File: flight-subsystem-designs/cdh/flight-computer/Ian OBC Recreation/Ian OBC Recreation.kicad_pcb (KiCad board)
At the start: 4 copper layers, 90 x 96 mm, 43 parts, among them J1 Conn_01x03, J2 Conn_01x03, J3 Conn_01x03, J4 Conn_01x03, J5 Conn_01x03, J6 Conn_01x03, J8 Conn_02x26_Odd_Even, Q1 AON6411, U1 BEAGLEBONEBLACK, U2 TPS2400DBVR, U3 TCAN337G, U4 MCP7940N-xSN, U5 ADM3485EARZ, U6 MAX706RESA+T, U7 TMP36xS

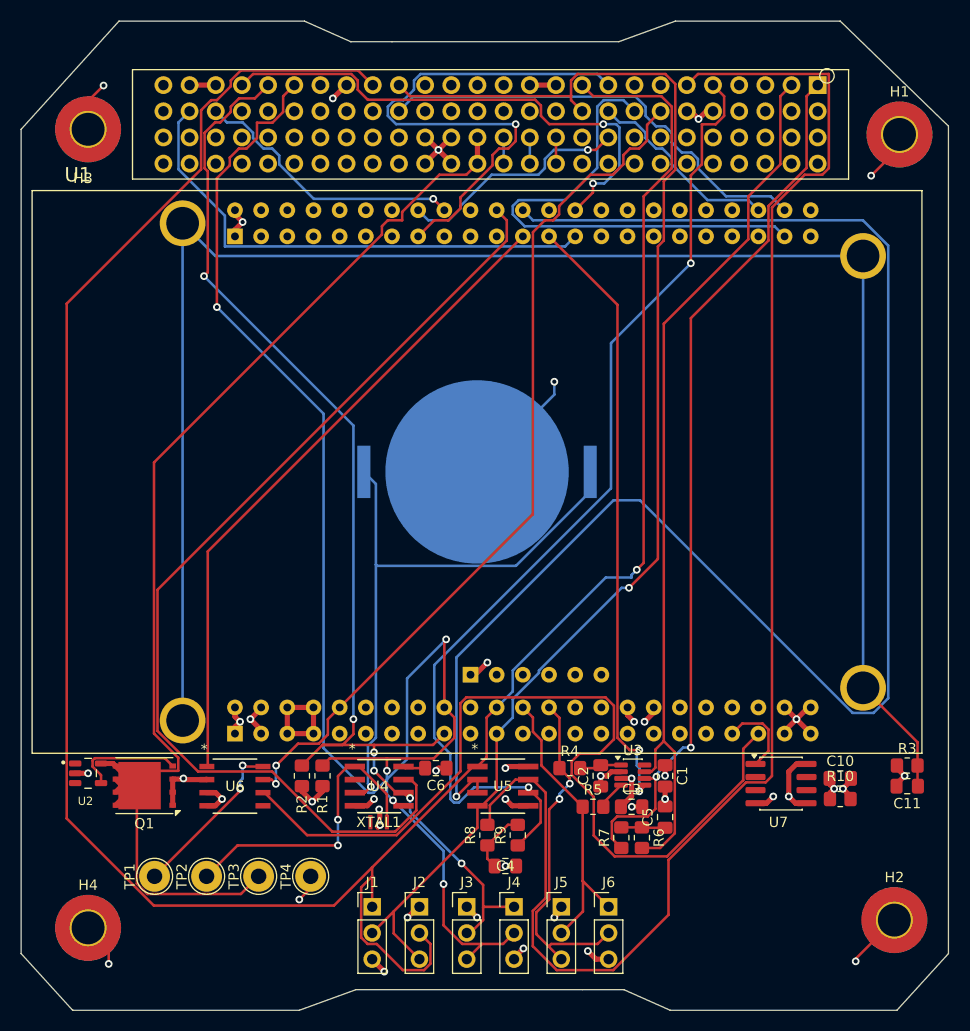
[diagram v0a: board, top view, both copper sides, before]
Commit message: Hashed down to warnings - Still not trustworthy
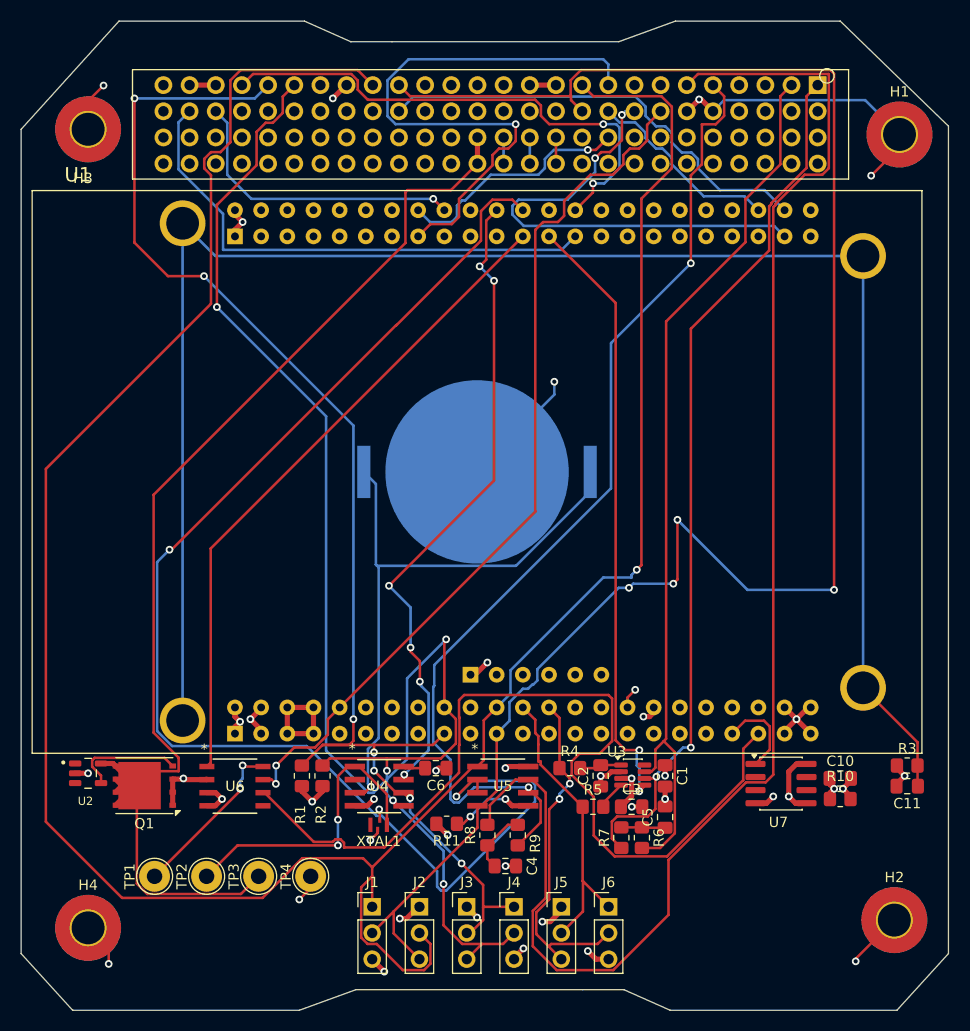
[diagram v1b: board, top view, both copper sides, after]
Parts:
- added R11: 10k, Resistor_SMD:R_0805_2012Metric_Pad1.20x1.40mm_HandSolder, F.Cu at (116.8, 117.4)
- moved XTAL1 0.25 mm to (110.2, 117.5)
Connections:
- U5 pad 5: GND -> Net-(U5-GND)
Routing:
- net /UART_TX: track 132.3 -> 176.4 mm, vias 1 -> 4
- net /RTCC_MFP: track 98.9 -> 63.4 mm, vias 0 -> 6
- net /GPIO1_1: track 155.7 -> 130.2 mm, vias 1 -> 2
- net GND: track 93.4 -> 108.7 mm, vias 30 -> 29
- net /I2C_SCL: track 118.6 -> 132.0 mm, vias 6 -> 7
- net Net-(U5-GND): track 0.00 -> 8.18 mm, vias 0 -> 2
- net /UART_RX: track 247.1 -> 251.2 mm
- net /GPIO1_15: track 53.5 -> 57.3 mm
- net /GPIO2_1: track 27.0 -> 29.1 mm
- net /GPIO3_20: track 85.4 -> 87.5 mm
- net /GPIO2_8: track 48.1 -> 46.0 mm, vias 0 -> 2
- net /GPIO1_14: track 22.8 -> 23.5 mm
- net VDD_3V3B: track 37.7 -> 38.3 mm
- net /GPIO2_22: track 49.8 -> 50.4 mm
- net /Temp: track 8.03 -> 8.60 mm

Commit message: OBC Version 6.1; no warnings, no errors (pcb)
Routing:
- net GND: track 108.7 -> 111.1 mm
- net /UART_TX: vias 4 -> 3
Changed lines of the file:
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@@
 		(tags "resistor handsolder")
 		(property "Reference" "R5"
-			(at 0 -1.65 0)
+			(at -1.1 1.75 0)
 			(layer "F.SilkS")
 			(effects
@@
 		)
 		(fp_text user "*"
-			(at -2.6162 -3.6068 0)
-			(layer "F.SilkS")
-			(effects
-				(font
-					(size 1 1)
-					(thickness 0.15)
-				)
-			)
-		)
-		(fp_text user "*"
-			(at -2.6162 -3.6068 0)
-			(unlocked yes)
-			(layer "F.SilkS")
-			(effects
-				(font
-					(size 1 1)
-					(thickness 0.15)
-				)
-			)
-		)
-		(fp_text user "*"
 			(at -1.5748 -2.3749 0)
 			(unlocked yes)
@@
 		(tags "resistor handsolder")
 		(property "Reference" "R6"
-			(at 0 -1.65 90)
+			(at 0.95 -2.05 90)
 			(layer "F.SilkS")
 			(effects
@@
 		(tags "TSOT TO_SOT_SMD")
 		(property "Reference" "U3"
-			(at -1.5625 -2.275 0)
+			(at -1.7625 -2.775 0)
 			(layer "F.SilkS")
 			(effects
 				(font
-					(size 1 1)
+					(size 0.8 0.8)
 					(thickness 0.15)
 				)
@@
 		(tags "capacitor handsolder")
 		(property "Reference" "C3"
-			(at 0 -1.68 0)
+			(at -2.85 1.65 0)
 			(layer "F.SilkS")
 			(effects
 				(font
-					(size 1 1)
+					(size 0.8 0.8)
 					(thickness 0.15)
 				)
@@
 		(tags "resistor handsolder")
 		(property "Reference" "R3"
-			(at 0 -1.65 0)
+			(at -1 -2.05 0)
 			(layer "F.SilkS")
 			(effects
@@
 		(tags "capacitor handsolder")
 		(property "Reference" "C2"
-			(at 0 -1.68 90)
+			(at -4.25 -3.45 90)
 			(layer "F.SilkS")
 			(effects
@@
 		(at 119.75 83.25)
 		(property "Reference" "U1"
-			(at -38.735 -28.834 0)
+			(at -40.55 -29.45 0)
 			(layer "F.SilkS")
 			(effects
@@
 			(layer "F.SilkS")
 		)
-		(fp_circle
-			(center -0.9 -0.9)
-			(end -0.2 -0.9)
-			(stroke
-				(width 0.12)
-				(type solid)
-			)
-			(fill no)
-			(layer "F.SilkS")
-		)
 		(fp_line
 			(start -2 67)
@@
 		)
 		(fp_text user "*"
-			(at -2.7178 -3.6068 0)
-			(unlocked yes)
-			(layer "F.SilkS")
-			(effects
-				(font
-					(size 1 1)
-					(thickness 0.15)
-				)
-			)
-		)
-		(fp_text user "*"
-			(at -2.7178 -3.6068 0)
-			(layer "F.SilkS")
-			(effects
-				(font
-					(size 1 1)
-					(thickness 0.15)
-				)
-			)
-		)
-		(fp_text user "*"
 			(at -1.6129 -2.4257 0)
 			(unlocked yes)
@@
 		(tags "capacitor handsolder")
 		(property "Reference" "C5"
-			(at 0 -1.68 90)
+			(at 0.261252 1.8 90)
 			(layer "F.SilkS")
 			(effects
@@
 			(layer "F.Fab")
 		)
-		(fp_text user "*"
-			(at -2.97815 -3.5814 0)
-			(unlocked yes)
-			(layer "F.SilkS")
-			(effects
-				(font
-					(size 1 1)
-					(thickness 0.15)
-				)
-			)
-		)
-		(fp_text user "*"
-			(at -2.97815 -3.5814 0)
-			(layer "F.SilkS")
-			(effects
-				(font
-					(size 1 1)
-					(thickness 0.15)
-				)
-			)
-		)
 		(fp_text user "${REFERENCE}"
 			(at 0 0 0)
@@
 		(tags "resistor handsolder")
 		(property "Reference" "R4"
-			(at 0 -1.65 0)
+			(at 1.75 -2.1 0)
 			(layer "F.SilkS")
 			(effects
 				(font
-					(size 1 1)
+					(size 0.8 0.8)
 					(thickness 0.15)
 				)
@@
 		(tags "resistor handsolder")
 		(property "Reference" "R10"
-			(at 0 -2.21 180)
+			(at 0.1 1.8 180)
 			(layer "F.SilkS")
 			(effects
@@
 	)
 	(segment
-		(start 96.255 107.995)
-		(end 96.75 107.5)
-		(width 0.5)
-		(layer "F.Cu")
-		(net 2)
-	)
-	(segment
 		(start 160.5 111.75)
 		(end 160.5 112)
@@
 	)
 	(segment
+		(start 95.86 107.4)
+		(end 96.255 107.005)
+		(width 0.5)
+		(layer "F.Cu")
+		(net 2)
+	)
+	(segment
 		(start 110.101024 118.298976)
 		(end 109.4 119)
@@
 	)
 	(segment
-		(start 96.255 106.11)
-		(end 96.255 107.005)
-		(width 0.5)
-		(layer "F.Cu")
-		(net 2)
-	)
-	(segment
 		(start 149.61 106.11)
 		(end 150.75 107.25)
@@
 	)
 	(segment
-		(start 96.255 108.65)
-		(end 96.255 107.995)
-		(width 0.5)
-		(layer "F.Cu")
-		(net 2)
-	)
-	(segment
 		(start 114.71 53.33)
 		(end 114.71 53.29)
@@
 	)
 	(segment
+		(start 95.66 107.4)
+		(end 96.255 107.995)
+		(width 0.5)
+		(layer "F.Cu")
+		(net 2)
+	)
+	(segment
 		(start 117.25 50.79)
 		(end 117.21 50.79)
@@
 	)
 	(segment
-		(start 96.255 107.005)
-		(end 96.75 107.5)
+		(start 94.6 107.4)
+		(end 95.66 107.4)
 		(width 0.5)
 		(layer "F.Cu")
@@
 	)
 	(segment
+		(start 96.255 107.995)
+		(end 96.255 108.65)
+		(width 0.5)
+		(layer "F.Cu")
+		(net 2)
+	)
+	(segment
 		(start 156 115)
 		(end 156 114.75)
@@
 	)
 	(segment
+		(start 96.255 107.005)
+		(end 96.255 106.11)
+		(width 0.5)
+		(layer "F.Cu")
+		(net 2)
+	)
+	(segment
 		(start 140.15 48.25)
 		(end 141.3 47.1)
@@
 	)
 	(segment
+		(start 94.6 107.4)
+		(end 95.86 107.4)
+		(width 0.5)
+		(layer "F.Cu")
+		(net 2)
+	)
+	(segment
 		(start 132.352728 112.765)
 		(end 131.75 112.765)
@@
 	)
 	(via
-		(at 96.75 107.5)
+		(at 94.6 107.4)
 		(size 0.75)
 		(drill 0.4)
@@
 		(size 0.75)
 		(drill 0.4)
-		(layers "F.Cu" "B.Cu")
-		(net 9)
-	)
-	(via
-		(at 134.5 94.5)
-		(size 0.75)
-		(drill 0.4)

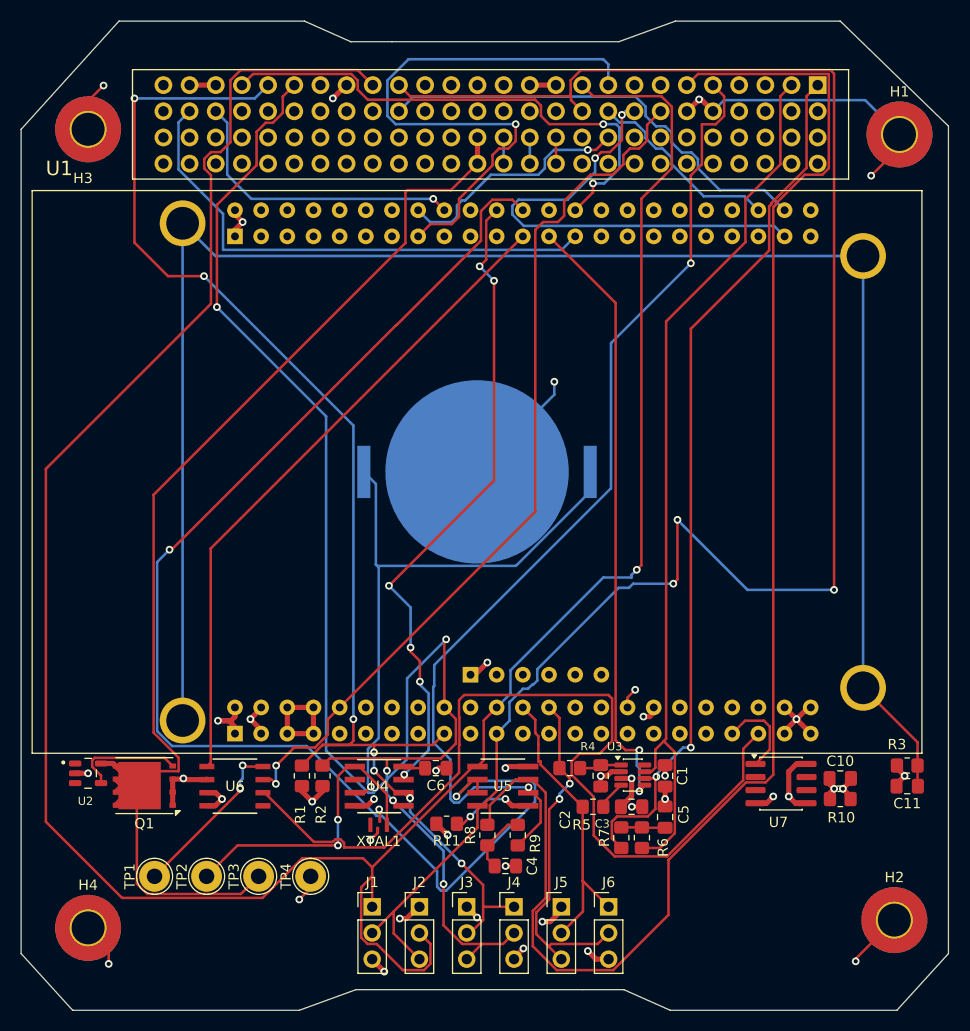
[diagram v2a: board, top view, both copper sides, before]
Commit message: DRC Friendly: Fixed Connectors
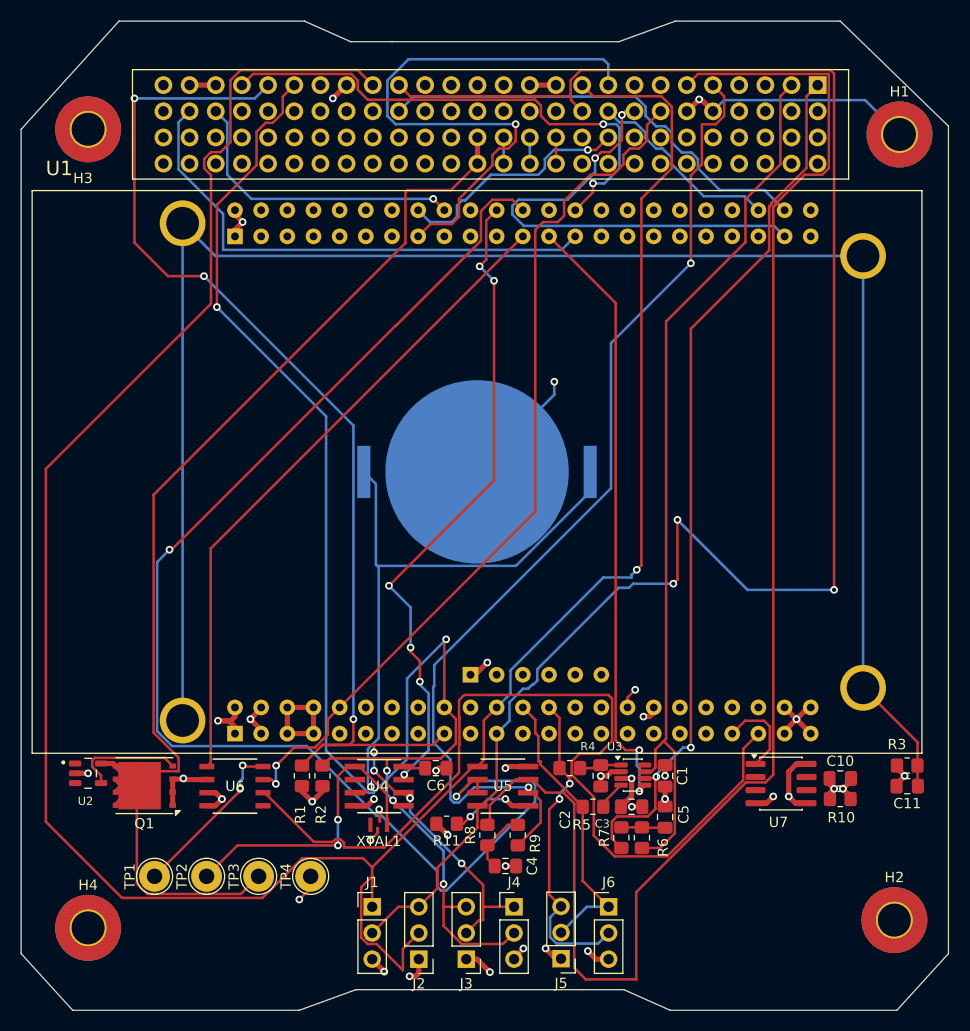
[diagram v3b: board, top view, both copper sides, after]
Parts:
- moved J2 5.08 mm to (114.1, 130.5), turned to 180 degrees
- moved J3 5.08 mm to (118.7, 130.5), turned to 180 degrees
- moved J5 5.04 mm to (127.9, 130.5), turned to 180 degrees
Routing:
- net GND: track 111.1 -> 91.9 mm, vias 29 -> 25
- net /UART_TX: track 176.4 -> 171.9 mm
- net /DCAN1TX: track 34.0 -> 31.2 mm
- net /UART_RX: track 251.2 -> 249.1 mm
- net /RS45B: track 145.1 -> 146.6 mm

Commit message: Routing is fixed unless I missed something
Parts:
- removed J1, J2, J3, J4, J5, J6: Conn_01x03, Connector_PinHeader_2.54mm:PinHeader_1x03_P2.54mm_Vertical
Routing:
- net /I2C_SDA: track 151.1 -> 124.9 mm, vias 5 -> 3
- net /DCAN1TX: track 31.2 -> 6.31 mm, vias 2 -> 0
- net /RS45B: track 146.6 -> 123.7 mm
- net /I2C_SCL: track 132.0 -> 111.2 mm, vias 7 -> 5
- net /DCAN1RX: track 28.6 -> 12.2 mm
- net /UART_RX: track 249.1 -> 233.1 mm
- net /UART_TX: track 171.9 -> 156.3 mm
- net GND: track 91.9 -> 79.2 mm, vias 25 -> 19
- net /3V3IN: track 115.8 -> 117.1 mm

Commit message: Intermediate fixes, still WIP
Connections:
- J8 pad 77: /5VIN -> SYS_5V
- J8 pad 78: /5VIN -> SYS_5V
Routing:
- net SYS_5V: track 10.2 -> 91.3 mm, vias 0 -> 1
- net /5VIN: track 2.54 -> 0.00 mm

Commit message: More Patches and 5V Re-Added
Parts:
- added Q2: AON6411, Package_DFN_QFN:AO_DFN-8-1EP_5.55x5.2mm_P1.27mm_EP4.12x4.6mm, F.Cu at (151.6, 122.5)
- added TP5: TestPoint, TestPoint:TestPoint_THTPad_D3.0mm_Drill1.5mm, F.Cu at (154.4, 130.7)
- added TP6: TestPoint, TestPoint:TestPoint_THTPad_D3.0mm_Drill1.5mm, F.Cu at (149.6, 130.7)
- added U8: TPS2400DBVR, Footprints:SOT95P280X145-5N, F.Cu at (156.8, 121.4)
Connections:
- J8 pad 77: SYS_5V -> /5VIN
- J8 pad 78: SYS_5V -> /5VIN
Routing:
- net /5VIN: track 0.00 -> 120.7 mm, vias 0 -> 5
- net Net-(Q2-G): track 0.00 -> 11.6 mm, vias 0 -> 2
- net SYS_5V: track 91.3 -> 82.4 mm, vias 1 -> 2
- net /UART_TX: track 156.3 -> 149.5 mm, vias 3 -> 1
- net GND: track 79.2 -> 81.9 mm, vias 19 -> 20
- net /RS45B: track 123.7 -> 125.0 mm

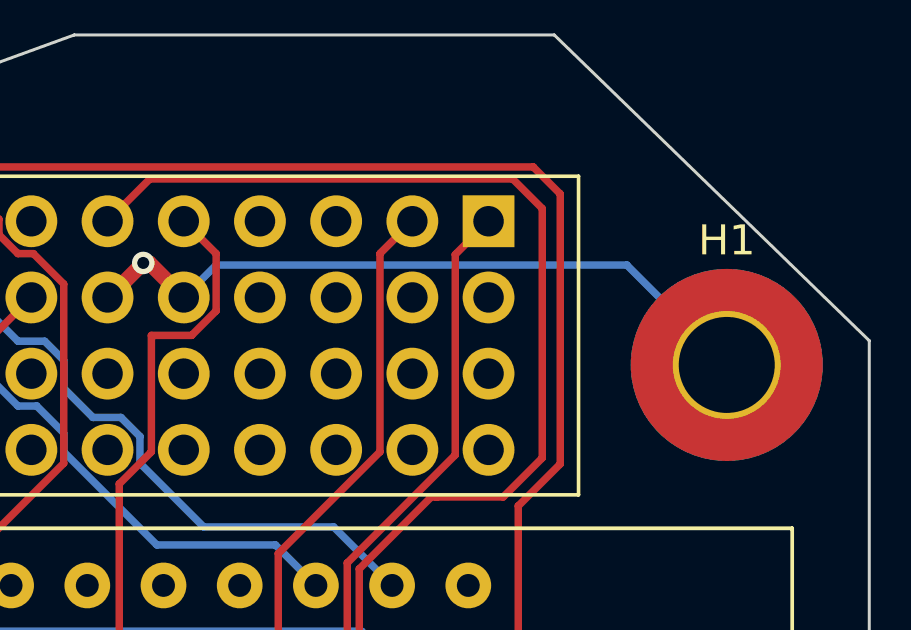
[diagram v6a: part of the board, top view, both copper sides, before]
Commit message: Mounting holes still need work
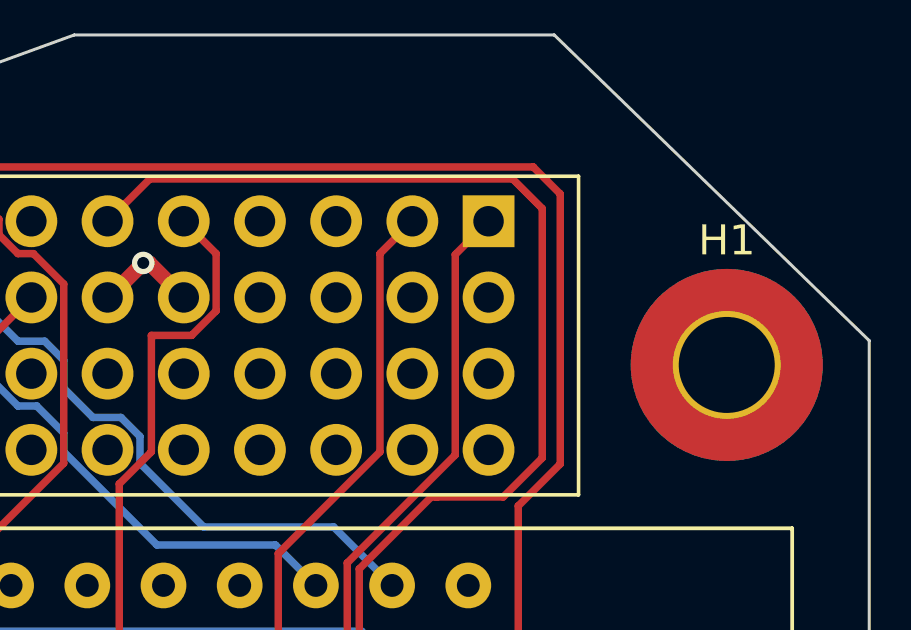
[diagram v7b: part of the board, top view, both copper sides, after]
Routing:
- net GND: track 81.9 -> 62.0 mm
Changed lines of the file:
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@@
-	)
-	(segment
-		(start 157.4204 47.1704)
-		(end 143.7296 47.1704)
-		(width 0.25)
-		(layer "B.Cu")
-		(net 2)
-	)
-	(segment
-		(start 160.75 50.5)
-		(end 157.4204 47.1704)
-		(width 0.25)
-		(layer "B.Cu")
-		(net 2)
 	)
 	(segment
@@
 		(width 0.25)
 		(layer "B.Cu")
-		(net 2)
-	)
-	(segment
-		(start 143.7296 47.1704)
-		(end 142.65 48.25)
-		(width 0.25)
-		(layer "B.Cu")
